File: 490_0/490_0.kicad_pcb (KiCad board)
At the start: 4 copper layers, 209.6 x 142.9 mm, 196 parts, among them J1 PAD, J10 PAD, J11 S3B-XH-A, J12 2000-1-1-20-00-BK, J13 S2B-ZR, J14 2000-1-1-20-00-BK, J15 S3B-XH-A, J16 DF40HC(3.0)-100DS-0.4V(58), J17 DF40HC(3.0)-100DS-0.4V(58), J18 TS-103-G-A, J2 PAD, J20 YO0201500000G, J21 TS-102-G-A, J22 2000-1-1-20-00-BK, J23 S3B-XH-A, J3 PAD, J4 PAD, J5 PAD, J6 PAD, J7 629105150521, J8 0526101571, J9 PAD, Q1 AO3400A, Q2 AO3400A, Q3 AO3400A, Q4 AO3400A, Q5 AO3400A, Q6 BSS84, SW1 TL2230EEF140, SW2 TL1105LF160Q, SW3 TL1105LF160Q, SW4 TL1105LF160Q, SW5 TL1105LF160Q, SW6 TL1105LF160Q, SW7 TL1105LF160Q, SW8 TL1105LF160Q, U1 MAX98357A, U10 EMI8142MUTAG, U11 SP3003-02XTG, U12 TPD8S009DSMR, U13 SP3003-02XTG, U14 SP3003-02XTG, U15 SP3003-02XTG, U16 SP3003-02XTG, U17 SP3003-02XTG, U18 TPD8S009DSMR, U19 SP3003-02XTG, U2 TPS2553DBVR, U3 TPS2553DBVR, U4 USB2512B-I/M2, U5 TS3USB221AQRSERQ1, U6 PCA9685, U7 TPS566247DRLR, U8 MP2639AGR-Z, U9 EMI8142MUTAG, Y1 24M20P2/XT324-10/10

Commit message: small push
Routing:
- net +5V: track 17.8 -> 19.1 mm, vias 3 -> 4
- net +3.3V: track 2.44 -> 3.52 mm, vias 5 -> 6
- net GND: vias 39 -> 40

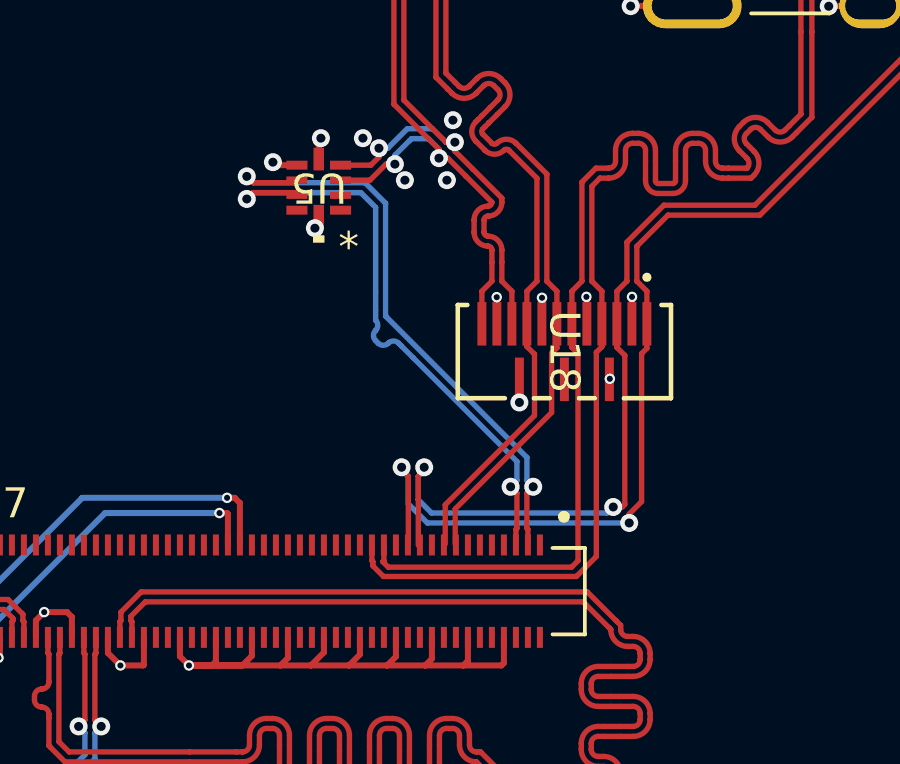
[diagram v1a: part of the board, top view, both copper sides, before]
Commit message: Routed the FFC HDMI to 100conn
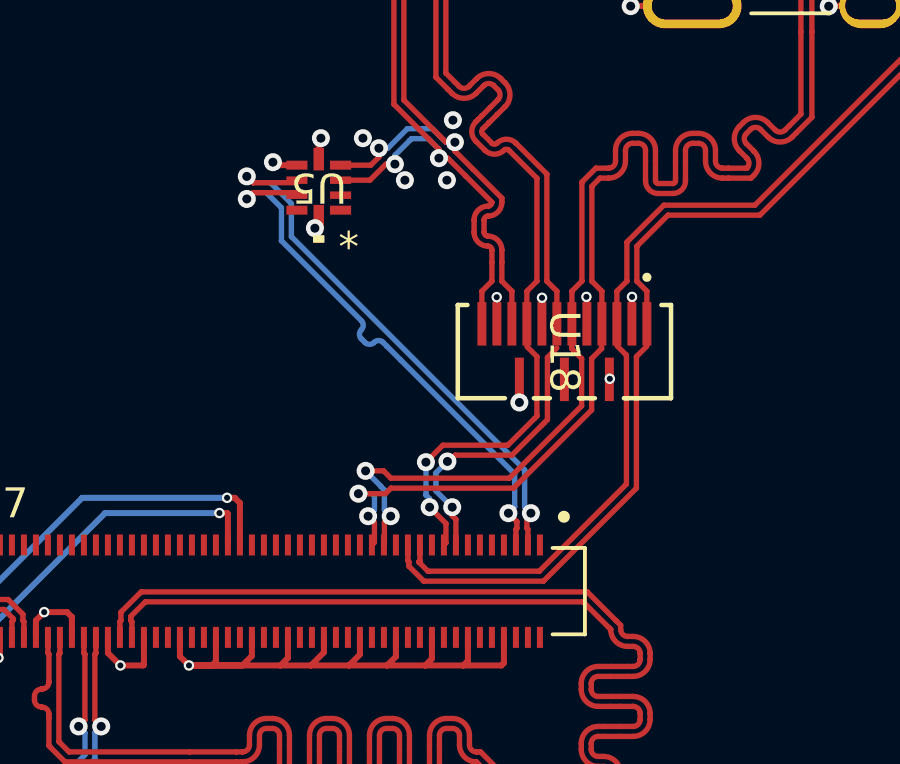
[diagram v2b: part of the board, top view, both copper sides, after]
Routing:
- net /PCB1/PCB1-Board Connector A/CAM1_D1_P: track 51.2 -> 47.6 mm, vias 2 -> 0
- net /PCB1/PCB1-Board Connector A/CAM1_D1_N: track 49.9 -> 46.5 mm, vias 2 -> 0
- net /PCB1/PCB1-Board Connector A/CAM1_C_P: track 49.2 -> 46.4 mm, vias 0 -> 2
- net /PCB1/PCB1-Board Connector A/USB_N: track 20.3 -> 18.4 mm
- net /PCB1/PCB1-Board Connector A/USB_P: track 20.2 -> 18.3 mm
- net /PCB1/PCB1-Board Connector A/CAM1_C_N: track 47.9 -> 46.1 mm, vias 0 -> 2
- net /PCB1/PCB1-Board Connector A/CAM1_D0_P: track 41.4 -> 42.6 mm, vias 0 -> 2
- net /PCB1/PCB1-Board Connector A/CAM1_D0_N: track 41.5 -> 42.4 mm, vias 0 -> 2

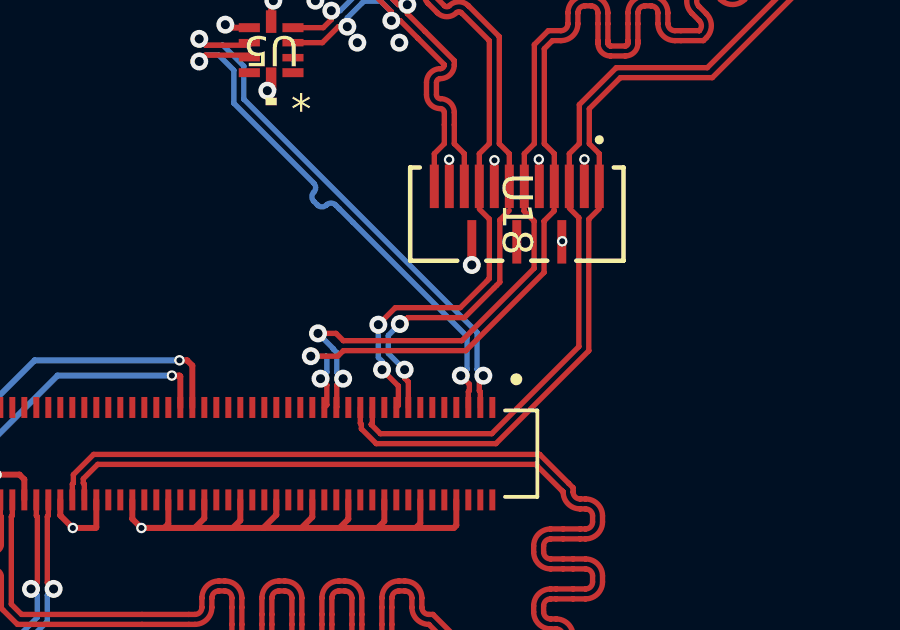
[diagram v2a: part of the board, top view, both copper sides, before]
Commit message: added a few grounds around signal vias
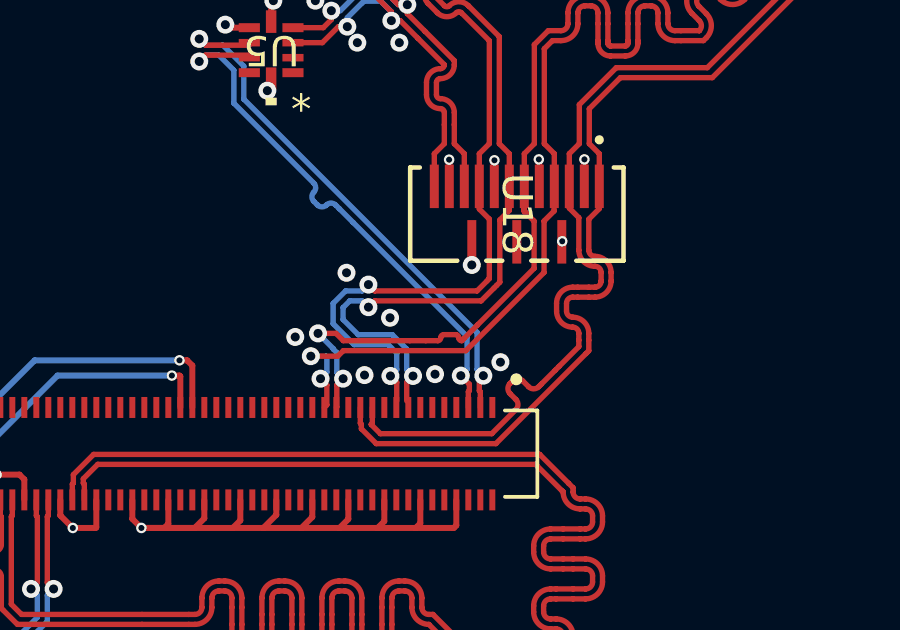
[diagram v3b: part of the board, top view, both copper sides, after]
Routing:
- net /PCB1/PCB1-Board Connector A/CAM1_D0_N: track 42.4 -> 46.6 mm
- net /PCB1/PCB1-Board Connector A/CAM1_D0_P: track 42.6 -> 46.7 mm
- net /PCB1/PCB1-Board Connector A/CAM1_D1_N: track 46.5 -> 50.2 mm
- net /PCB1/PCB1-Board Connector A/CAM1_D1_P: track 47.6 -> 50.3 mm
- net /PCB1/PCB1-Board Connector A/CAM1_C_N: track 46.1 -> 47.2 mm
- net /PCB1/PCB1-Board Connector A/CAM1_C_P: track 46.4 -> 47.1 mm
- net GND: vias 40 -> 46

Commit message: Place CM4 footprint, starting to reroute everything
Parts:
- removed H1, H2, H3, H4: MountingHole, MountingHole:MountingHole_3mm
- added ?: , clipboard:099e6188-6dd9-4ba0-b053-8b541a3ab987, F.Cu at (90.5, 137.7)
- moved J7 287.4 mm to (98.8, 86.3), turned to 180 degrees
- moved J18 286.5 mm to (96.5, 98.8), turned to 180 degrees
- moved U11 281.3 mm to (99.1, 92.8), turned to 90 degrees
- moved C6 274.6 mm to (92.0, 91.6), turned to 180 degrees
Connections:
- net Net-(J7-D+) renamed /PCB1/PCB1-Charging and Power Port + USB switch/MICROD+
- net Net-(J7-D-) renamed /PCB1/PCB1-Charging and Power Port + USB switch/MICROD-
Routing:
- net /PCB1/PCB1-Charging and Power Port + USB switch/MICROD+: track 0.00 -> 61.4 mm, vias 0 -> 2
- net /PCB1/PCB1-Charging and Power Port + USB switch/MICROD-: track 0.00 -> 61.4 mm, vias 0 -> 2
- net /PCB1/PCB1-Board Connector A/Camera_GPIO: track 3.30 -> 31.2 mm, vias 0 -> 2
- net /PCB1/PCB1-Board Connector A/SDA1: track 9.43 -> 29.7 mm, vias 0 -> 2
- net /PCB1/PCB1-Board Connector A/SCL1: track 3.69 -> 20.8 mm, vias 0 -> 2
- net /PCB1/PCB1-Board Connector A/HDMI0_SCL: track 21.2 -> 19.1 mm
- net /PCB1/PCB1-Board Connector A/HDMI0_HOTPLUG: track 30.5 -> 28.6 mm
- net /PCB1/PCB1-Board Connector A/HDMI0_CEC: track 38.0 -> 39.6 mm
- net /PCB1/PCB1-Board Connector A/HDMI0_SDA: track 35.9 -> 35.3 mm
